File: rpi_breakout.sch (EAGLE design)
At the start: 25 parts

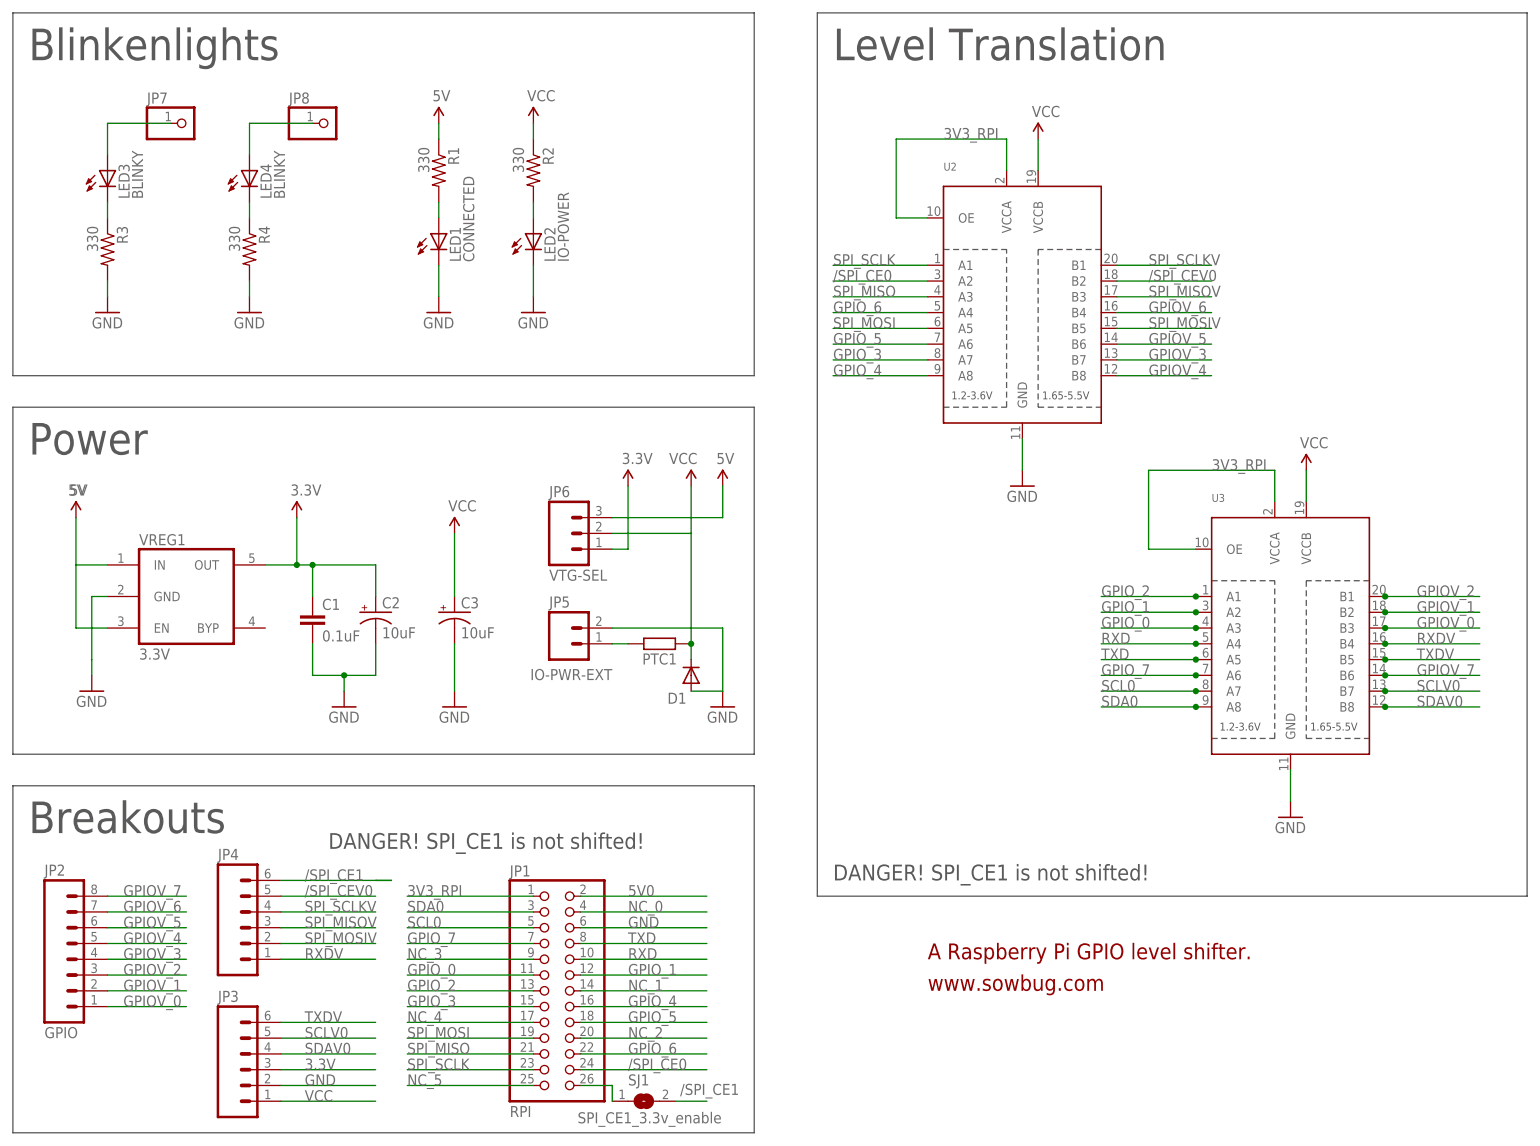
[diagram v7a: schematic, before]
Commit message: SCL/SDA pullup, 4.7K. GPIO labels are back.
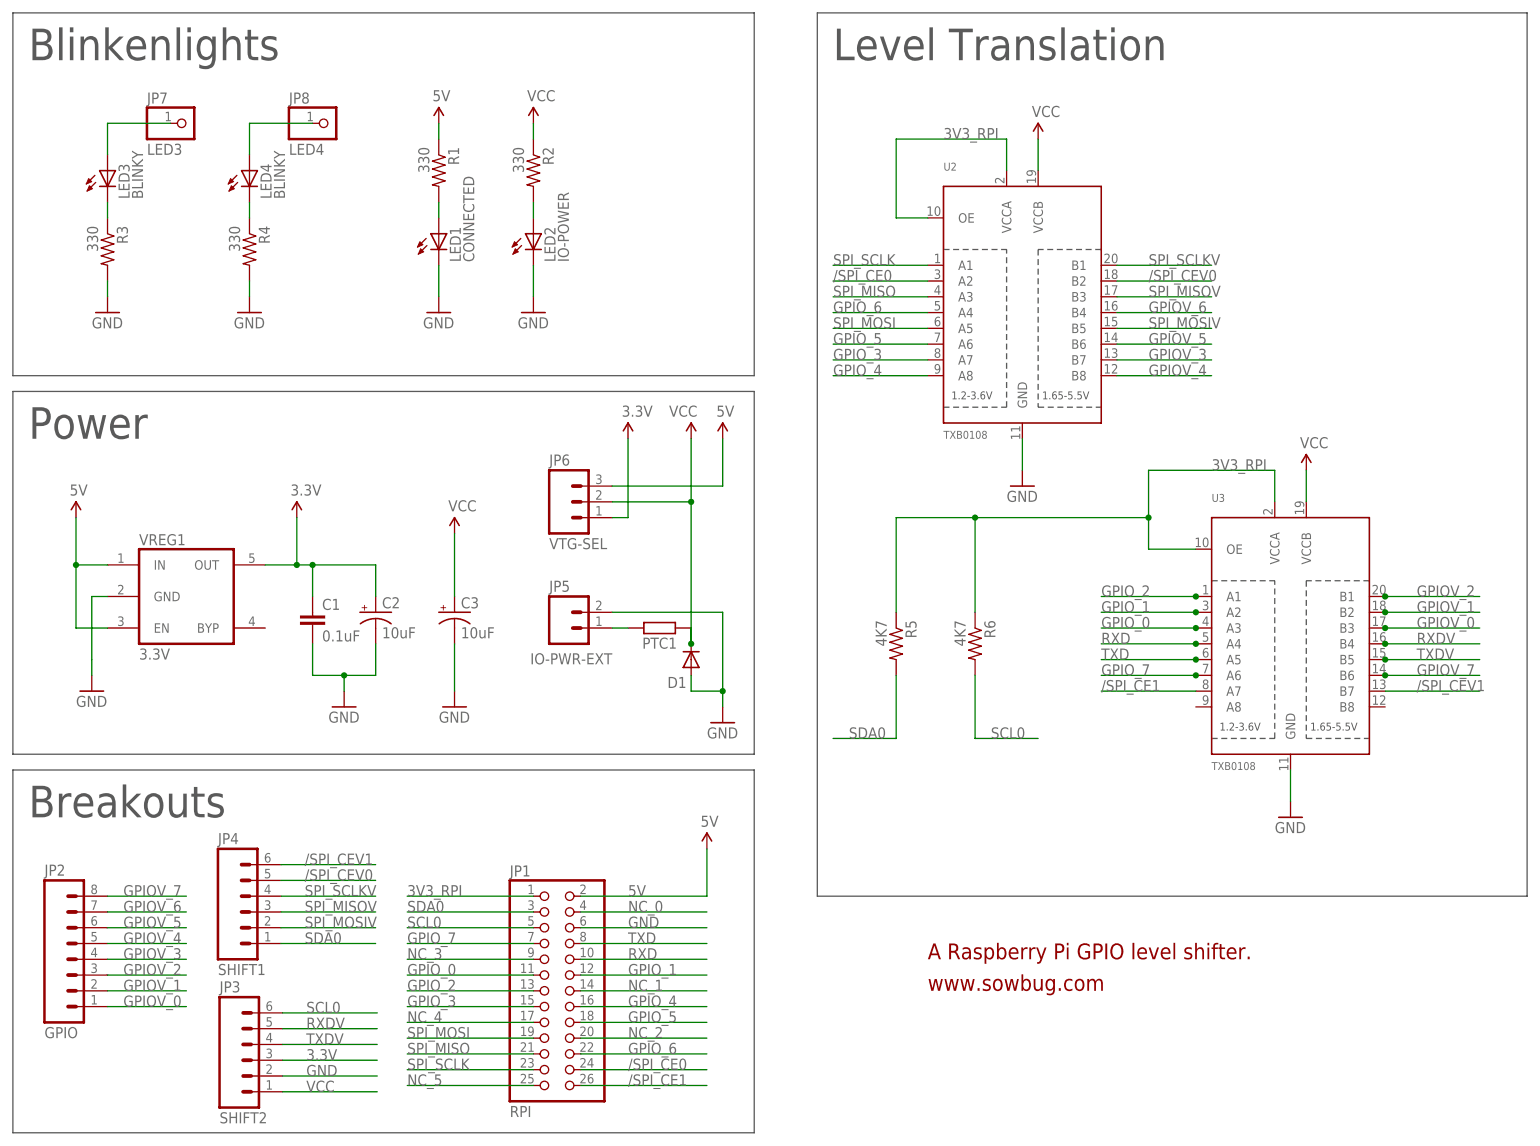
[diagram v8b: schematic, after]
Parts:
- removed SJ1: SPI_CE1_3.3v_enable, jumper:SJ
- added R5, R6: 4K7, SparkFun:RESISTOR0805-RES
- JP3: value (none) -> SHIFT2
- JP4: value (none) -> SHIFT1
- JP7: value (none) -> LED3
- JP8: value (none) -> LED4
- U2, U3: value (none) -> TXB0108
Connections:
- net N$6 renamed VCC_FUSE
- removed net 5V0: JP1.2
- removed net N$5: JP1.26, SJ1.1
- removed net SCLV0: JP3.5, U3.B7
- removed net SDAV0: JP3.4, U3.B8
- new net /SPI_CEV1: JP4.6, U3.B7
- net /SPI_CE1: now also JP1.26, U3.A7; no longer JP4.6, SJ1.2
- net 3V3_RPI: now also R5.1, R6.1
- net 5V: now also JP1.2
- net RXDV: now also JP3.5; no longer JP4.1
- net SCL0: now also JP3.6, R6.2; no longer U3.A7
- net SDA0: now also JP4.1, R5.2; no longer U3.A8
- net TXDV: now also JP3.4; no longer JP3.6
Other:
- note removed: "DANGER! SPI_CE1 is not shifted!"
- moved on the sheet: D1, JP3, JP4, JP5, JP6, PTC1
